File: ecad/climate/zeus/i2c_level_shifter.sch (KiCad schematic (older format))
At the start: 9 parts, among them Q1 BSS138, Q2 BSS138, Q3 BSS138

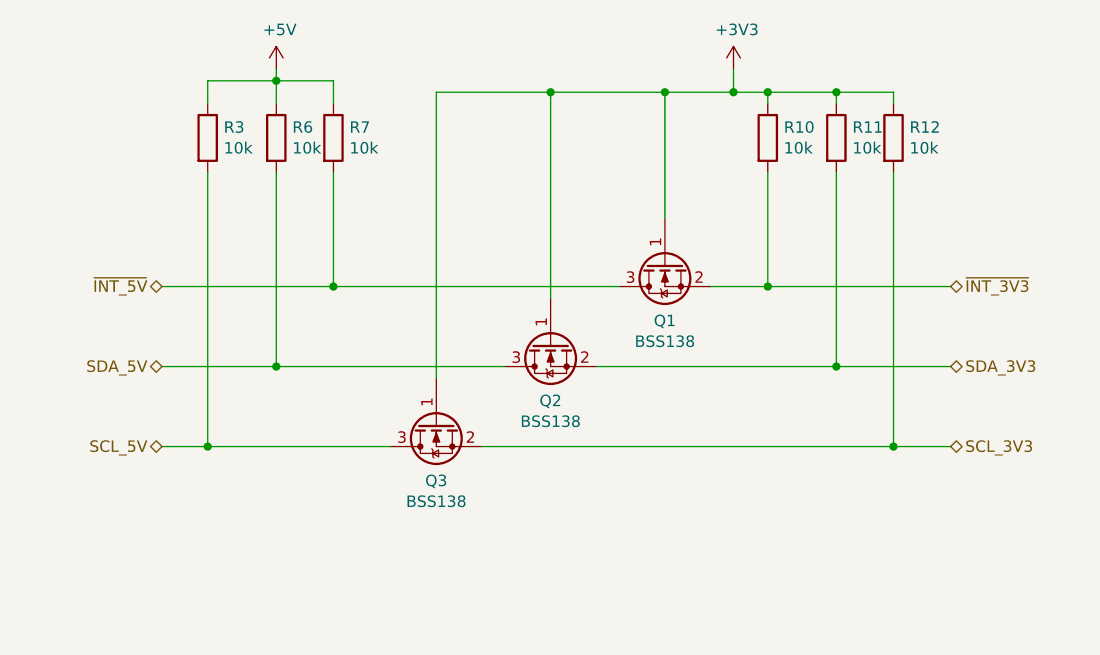
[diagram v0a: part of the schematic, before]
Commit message: Updates climate board to rev B~dev
 * Changes all Power Connectors to MiniFit-JR 5566-02A to avoid
   someone pluging the power supply on the CAN bus as it will destroy
   all MCP2561 on the bus
 * Fixes issues in Arke:
 ** Crossed Rx/Tx lines
 ** Flipped DB9 connector
 * Fixes and Improvment in Celaeno/Zeus:
 ** Added missing pull-up resistor on tachometer inputs
 ** Removed unecessary 32.268kHz oscillators (they are not working
    properly with manual soldering)
 ** Removed I2C multiplexer as we can add a second EMC2302 with a
   different i2c address to do the same thing. Repaced it by an i2c
   level shifter (tested and working).

Many of these changes still need to be tested before going to
production
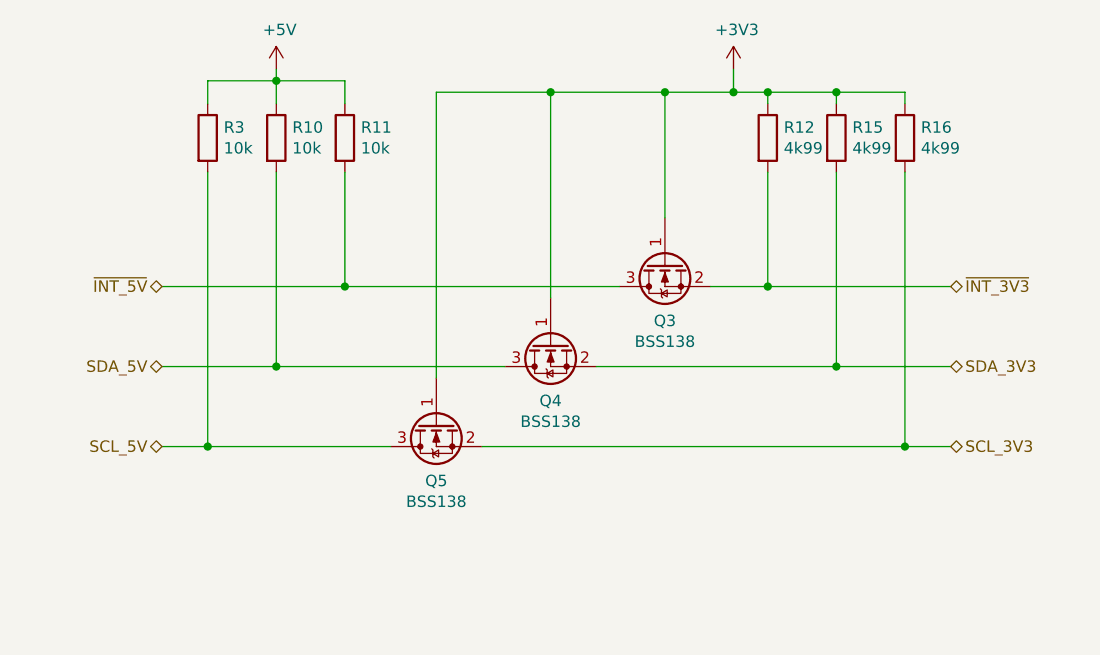
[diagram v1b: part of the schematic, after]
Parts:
- R12: renamed from R10; value 10k -> 4k99; Part Number GPR060310K -> GPR06034K99
- R15: renamed from R11; value 10k -> 4k99; Part Number GPR060310K -> GPR06034K99
- R16: renamed from R12; value 10k -> 4k99; Part Number GPR060310K -> GPR06034K99
- renumbered Q1 to Q3, Q2 to Q4, Q3 to Q5, R6 to R10, R7 to R11
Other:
- moved on the sheet: R11, R16
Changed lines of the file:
@@
 EESchema Schematic File Version 4
-LIBS:celaeno-cache
+LIBS:zeus-cache
 EELAYER 26 0
 EELAYER END
 $Descr A4 11693 8268
 encoding utf-8
-Sheet 6 8
+Sheet 9 9
 Title "I2C 5V / 3V3 Level Shifter"
 Date "06/11/2018"
@@
 $EndDescr
 $Comp
-L Transistor_FET:BSS138 Q3
+L Transistor_FET:BSS138 Q5
 U 1 1 5BB396C4
 P 5800 3750
-F 0 "Q3" V 6050 3750 50  0000 C CNN
+F 0 "Q5" V 6050 3750 50  0000 C CNN
 F 1 "BSS138" V 6141 3750 50  0000 C CNN
 F 2 "Package_TO_SOT_SMD:SOT-23" H 6000 3675 50  0001 L CIN
@@
 $EndComp
 $Comp
-L power:+3V3 #PWR09
+L power:+3V3 #PWR0117
 U 1 1 5BB3983E
 P 7100 2200
-F 0 "#PWR09" H 7100 2050 50  0001 C CNN
+F 0 "#PWR0117" H 7100 2050 50  0001 C CNN
 F 1 "+3V3" H 7115 2373 50  0000 C CNN
 F 2 "" H 7100 2200 50  0001 C CNN
@@
 $EndComp
 $Comp
-L Transistor_FET:BSS138 Q2
+L Transistor_FET:BSS138 Q4
 U 1 1 5BB39855
 P 6300 3400
-F 0 "Q2" V 6550 3400 50  0000 C CNN
+F 0 "Q4" V 6550 3400 50  0000 C CNN
 F 1 "BSS138" V 6641 3400 50  0000 C CNN
 F 2 "Package_TO_SOT_SMD:SOT-23" H 6500 3325 50  0001 L CIN
@@
 $EndComp
 $Comp
-L Device:R R6
+L Device:R R10
 U 1 1 5BB39A93
 P 5100 2500
-F 0 "R6" H 5170 2546 50  0000 L CNN
+F 0 "R10" H 5170 2546 50  0000 L CNN
 F 1 "10k" H 5170 2455 50  0000 L CNN
 F 2 "Resistor_SMD:R_0603_1608Metric" V 5030 2500 50  0001 C CNN
@@
 $EndComp
 $Comp
-L Device:R R11
+L Device:R R15
 U 1 1 5BB39C33
 P 7550 2500
-F 0 "R11" H 7620 2546 50  0000 L CNN
-F 1 "10k" H 7620 2455 50  0000 L CNN
+F 0 "R15" H 7620 2546 50  0000 L CNN
+F 1 "4k99" H 7620 2455 50  0000 L CNN
 F 2 "Resistor_SMD:R_0603_1608Metric" V 7480 2500 50  0001 C CNN
 F 3 "~" H 7550 2500 50  0001 C CNN
-F 4 "GPR060310K" H 7550 2500 50  0001 C CNN "Part Number"
+F 4 "GPR06034K99" H 7550 2500 50  0001 C CNN "Part Number"
 	1    7550 2500
 	1    0    0    -1
 $EndComp
 $Comp
-L Device:R R12
+L Device:R R16
 U 1 1 5BB39C3B
-P 7800 2500
-F 0 "R12" H 7870 2546 50  0000 L CNN
-F 1 "10k" H 7870 2455 50  0000 L CNN
-F 2 "Resistor_SMD:R_0603_1608Metric" V 7730 2500 50  0001 C CNN
-F 3 "~" H 7800 2500 50  0001 C CNN
-F 4 "GPR060310K" H 7800 2500 50  0001 C CNN "Part Number"
-	1    7800 2500
+P 7850 2500
+F 0 "R16" H 7920 2546 50  0000 L CNN
+F 1 "4k99" H 7920 2455 50  0000 L CNN
+F 2 "Resistor_SMD:R_0603_1608Metric" V 7780 2500 50  0001 C CNN
+F 3 "~" H 7850 2500 50  0001 C CNN
+F 4 "GPR06034K99" H 7850 2500 50  0001 C CNN "Part Number"
+	1    7850 2500
 	1    0    0    -1
 $EndComp
@@
 	7550 3500 6500 3500
 Wire Wire Line
-	7800 2650 7800 3850
-Wire Wire Line
-	7800 3850 6000 3850
+	7850 2650 7850 3850
 Wire Wire Line
 	5100 2650 5100 3500
@@
 Connection ~ 7550 3500
 Wire Wire Line
-	7800 3850 8050 3850
-Connection ~ 7800 3850
-Wire Wire Line
 	7550 2300 7550 2350
 Wire Wire Line
-	7550 2300 7800 2300
-Wire Wire Line
-	7800 2300 7800 2350
-Connection ~ 7550 2300
+	7850 2300 7850 2350
 Text Notes 550  7750 0    50   ~ 0
 © 2018 Université de Lausanne\n\nThis documentation describes Open Hardware and is licensed under the\nCERN OHL v. 1.2.\n\nYou may redistribute and modify this documentation under the terms of\nthe CERN OHL v.1.2. (http://ohwr.org/cernohl). This documentation is\ndistributed WITHOUT ANY EXPRESS OR IMPLIED WARRANTY,\nINCLUDING OF MERCHANTABILITY, SATISFACTORY QUALITY AND\nFITNESS FOR A PARTICULAR PURPOSE. Please see the CERN OHL v.1.2\nfor applicable conditions
 Wire Wire Line
-	5100 2250 5350 2250
-Wire Wire Line
-	5350 2250 5350 2350
-$Comp
-L Device:R R7
+	5400 2250 5400 2350
+$Comp
+L Device:R R11
 U 1 1 5BB39AC5
-P 5350 2500
-F 0 "R7" H 5420 2546 50  0000 L CNN
-F 1 "10k" H 5420 2455 50  0000 L CNN
-F 2 "Resistor_SMD:R_0603_1608Metric" V 5280 2500 50  0001 C CNN
-F 3 "~" H 5350 2500 50  0001 C CNN
-F 4 "GPR060310K" H 5350 2500 50  0001 C CNN "Part Number"
-	1    5350 2500
+P 5400 2500
+F 0 "R11" H 5470 2546 50  0000 L CNN
+F 1 "10k" H 5470 2455 50  0000 L CNN
+F 2 "Resistor_SMD:R_0603_1608Metric" V 5330 2500 50  0001 C CNN
+F 3 "~" H 5400 2500 50  0001 C CNN
+F 4 "GPR060310K" H 5400 2500 50  0001 C CNN "Part Number"
+	1    5400 2500
 	1    0    0    -1
 $EndComp
@@
 	7250 2300 7250 2350
 $Comp
-L Device:R R10
+L Device:R R12
 U 1 1 5BB39C2B
 P 7250 2500
-F 0 "R10" H 7320 2546 50  0000 L CNN
-F 1 "10k" H 7320 2455 50  0000 L CNN
+F 0 "R12" H 7320 2546 50  0000 L CNN
+F 1 "4k99" H 7320 2455 50  0000 L CNN
 F 2 "Resistor_SMD:R_0603_1608Metric" V 7180 2500 50  0001 C CNN
 F 3 "~" H 7250 2500 50  0001 C CNN
-F 4 "GPR060310K" H 7250 2500 50  0001 C CNN "Part Number"
+F 4 "GPR06034K99" H 7250 2500 50  0001 C CNN "Part Number"
 	1    7250 2500
 	1    0    0    -1
@@
 	6800 2850 6800 2300
 $Comp
-L Transistor_FET:BSS138 Q1
+L Transistor_FET:BSS138 Q3
 U 1 1 5BB3988D
 P 6800 3050
-F 0 "Q1" V 7050 3050 50  0000 C CNN
+F 0 "Q3" V 7050 3050 50  0000 C CNN
 F 1 "BSS138" V 7141 3050 50  0000 C CNN
 F 2 "Package_TO_SOT_SMD:SOT-23" H 7000 2975 50  0001 L CIN
@@
 $EndComp
 Wire Wire Line
-	6600 3150 5350 3150
-Wire Wire Line
-	5350 3150 5350 2650
-Connection ~ 5350 3150
-Wire Wire Line
-	4600 3150 5350 3150
+	6600 3150 5400 3150
+Wire Wire Line
+	5400 3150 5400 2650
 Text HLabel 4600 3150 0    50   BiDi ~ 0
 ~INT_5V
+Connection ~ 7850 3850
+Wire Wire Line
+	7850 3850 8050 3850
+Wire Wire Line
+	6000 3850 7850 3850
+Wire Wire Line
+	7550 2300 7850 2300
+Connection ~ 7550 2300
+Connection ~ 5400 3150
+Wire Wire Line
+	4600 3150 5400 3150
+Wire Wire Line
+	5100 2250 5400 2250
 $EndSCHEMATC

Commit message: Updates board for manufacturing
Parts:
- R12, R15, R16: value 4k99 -> 3k3; Part Number GPR06034K99 -> GPR06033K3
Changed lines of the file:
@@
 F 1 "10k" H 4870 2455 50  0000 L CNN
 F 2 "Resistor_SMD:R_0603_1608Metric" V 4730 2500 50  0001 C CNN
-F 3 "~" H 4800 2500 50  0001 C CNN
+F 3 "" H 4800 2500 50  0001 C CNN
 F 4 "GPR060310K" H 4800 2500 50  0001 C CNN "Part Number"
 	1    4800 2500
@@
 F 1 "10k" H 5170 2455 50  0000 L CNN
 F 2 "Resistor_SMD:R_0603_1608Metric" V 5030 2500 50  0001 C CNN
-F 3 "~" H 5100 2500 50  0001 C CNN
+F 3 "" H 5100 2500 50  0001 C CNN
 F 4 "GPR060310K" H 5100 2500 50  0001 C CNN "Part Number"
 	1    5100 2500
@@
 P 7550 2500
 F 0 "R15" H 7620 2546 50  0000 L CNN
-F 1 "4k99" H 7620 2455 50  0000 L CNN
+F 1 "3k3" H 7620 2455 50  0000 L CNN
 F 2 "Resistor_SMD:R_0603_1608Metric" V 7480 2500 50  0001 C CNN
-F 3 "~" H 7550 2500 50  0001 C CNN
-F 4 "GPR06034K99" H 7550 2500 50  0001 C CNN "Part Number"
+F 3 "" H 7550 2500 50  0001 C CNN
+F 4 "GPR06033K3" H 7550 2500 50  0001 C CNN "Part Number"
 	1    7550 2500
 	1    0    0    -1
@@
 P 7850 2500
 F 0 "R16" H 7920 2546 50  0000 L CNN
-F 1 "4k99" H 7920 2455 50  0000 L CNN
+F 1 "3k3" H 7920 2455 50  0000 L CNN
 F 2 "Resistor_SMD:R_0603_1608Metric" V 7780 2500 50  0001 C CNN
-F 3 "~" H 7850 2500 50  0001 C CNN
-F 4 "GPR06034K99" H 7850 2500 50  0001 C CNN "Part Number"
+F 3 "" H 7850 2500 50  0001 C CNN
+F 4 "GPR06033K3" H 7850 2500 50  0001 C CNN "Part Number"
 	1    7850 2500
 	1    0    0    -1
@@
 F 1 "10k" H 5470 2455 50  0000 L CNN
 F 2 "Resistor_SMD:R_0603_1608Metric" V 5330 2500 50  0001 C CNN
-F 3 "~" H 5400 2500 50  0001 C CNN
+F 3 "" H 5400 2500 50  0001 C CNN
 F 4 "GPR060310K" H 5400 2500 50  0001 C CNN "Part Number"
 	1    5400 2500
@@
 P 7250 2500
 F 0 "R12" H 7320 2546 50  0000 L CNN
-F 1 "4k99" H 7320 2455 50  0000 L CNN
+F 1 "3k3" H 7320 2455 50  0000 L CNN
 F 2 "Resistor_SMD:R_0603_1608Metric" V 7180 2500 50  0001 C CNN
-F 3 "~" H 7250 2500 50  0001 C CNN
-F 4 "GPR06034K99" H 7250 2500 50  0001 C CNN "Part Number"
+F 3 "" H 7250 2500 50  0001 C CNN
+F 4 "GPR06033K3" H 7250 2500 50  0001 C CNN "Part Number"
 	1    7250 2500
 	1    0    0    -1

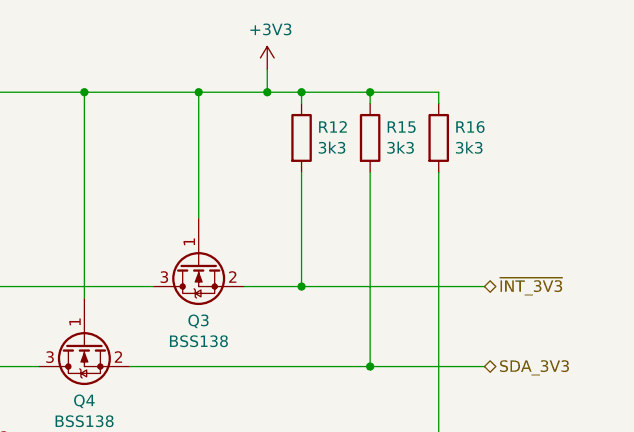
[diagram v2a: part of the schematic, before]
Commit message: Updates ecad for assembly production
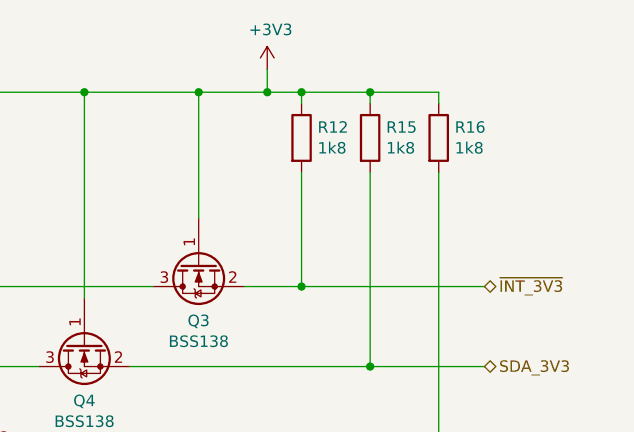
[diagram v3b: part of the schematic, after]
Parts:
- R12, R15, R16: value 3k3 -> 1k8; Part Number GPR06033K3 -> GPR06031K8
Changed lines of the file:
@@
-	1    0    0    -1
-$EndComp
-$Comp
-L Device:R R15
-U 1 1 5BB39C33
-P 7550 2500
-F 0 "R15" H 7620 2546 50  0000 L CNN
-F 1 "3k3" H 7620 2455 50  0000 L CNN
-F 2 "Resistor_SMD:R_0603_1608Metric" V 7480 2500 50  0001 C CNN
-F 3 "" H 7550 2500 50  0001 C CNN
-F 4 "GPR06033K3" H 7550 2500 50  0001 C CNN "Part Number"
-	1    7550 2500
-	1    0    0    -1
-$EndComp
-$Comp
-L Device:R R16
-U 1 1 5BB39C3B
-P 7850 2500
-F 0 "R16" H 7920 2546 50  0000 L CNN
-F 1 "3k3" H 7920 2455 50  0000 L CNN
-F 2 "Resistor_SMD:R_0603_1608Metric" V 7780 2500 50  0001 C CNN
-F 3 "" H 7850 2500 50  0001 C CNN
-F 4 "GPR06033K3" H 7850 2500 50  0001 C CNN "Part Number"
-	1    7850 2500
 	1    0    0    -1
 $EndComp
@@
 P 7250 2500
 F 0 "R12" H 7320 2546 50  0000 L CNN
-F 1 "3k3" H 7320 2455 50  0000 L CNN
+F 1 "1k8" H 7320 2455 50  0000 L CNN
 F 2 "Resistor_SMD:R_0603_1608Metric" V 7180 2500 50  0001 C CNN
 F 3 "" H 7250 2500 50  0001 C CNN
-F 4 "GPR06033K3" H 7250 2500 50  0001 C CNN "Part Number"
+F 4 "GPR06031K8" H 7250 2500 50  0001 C CNN "Part Number"
 	1    7250 2500
 	1    0    0    -1
@@
 Wire Wire Line
 	5100 2250 5400 2250
+$Comp
+L Device:R R15
+U 1 1 5C7D7026
+P 7550 2500
+F 0 "R15" H 7620 2546 50  0000 L CNN
+F 1 "1k8" H 7620 2455 50  0000 L CNN
+F 2 "Resistor_SMD:R_0603_1608Metric" V 7480 2500 50  0001 C CNN
+F 3 "" H 7550 2500 50  0001 C CNN
+F 4 "GPR06031K8" H 7550 2500 50  0001 C CNN "Part Number"
+	1    7550 2500
+	1    0    0    -1
+$EndComp
+$Comp
+L Device:R R16
+U 1 1 5C7D7050
+P 7850 2500
+F 0 "R16" H 7920 2546 50  0000 L CNN
+F 1 "1k8" H 7920 2455 50  0000 L CNN
+F 2 "Resistor_SMD:R_0603_1608Metric" V 7780 2500 50  0001 C CNN
+F 3 "" H 7850 2500 50  0001 C CNN
+F 4 "GPR06031K8" H 7850 2500 50  0001 C CNN "Part Number"
+	1    7850 2500
+	1    0    0    -1
+$EndComp
 $EndSCHEMATC
